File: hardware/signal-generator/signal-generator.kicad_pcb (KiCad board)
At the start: 4 copper layers, 135 parts, among them J1 AVR-ISP-6, J10 Output_Conn, J11 SD_Card_Conn, J12 TP_Conn, J13 LCD_Conn, J2 AVR_SPI, J3 PORT_G, J4 PORT_F, J5 PORT_E, J6 PORT_A, J7 PORT_C, J8 AREF, J9 Power_Supply_Rails, Q1 AP2310GN, Q2 AP2310GN, Q3 AP2310GN, Q4 AP2310GN, Q5 AP2310GN, Q6 AP2310GN, Q7 AP2310GN, Q8 AP2310GN, Q9 AP2310GN, SW1 RESET_BUTTON, U1 74HC04, U10 MCP23017-E/SO, U11 AD9764AR, U12 TS4061AICT-1.25, U13 74HC4040, U14 74HC4040, U15 MCP4651-502E/ST, U16 AZ431AN-A, U17 AD8021ARZ, U18 MCP4551-103E/MS, U19 AD8021ARZ, U2 74HC08, U20 AD8021ARZ, U21 AD8021ARZ, U3 74HC08, U4 74HC30, U5 ATmega2561-16AU, U6 ADP7142AUJZ-5.0, U7 TC1017-3.3VCTTR, U8 DS1085Z-10+, U9 CY7C1021D-10ZSXI, Y1 16MHz

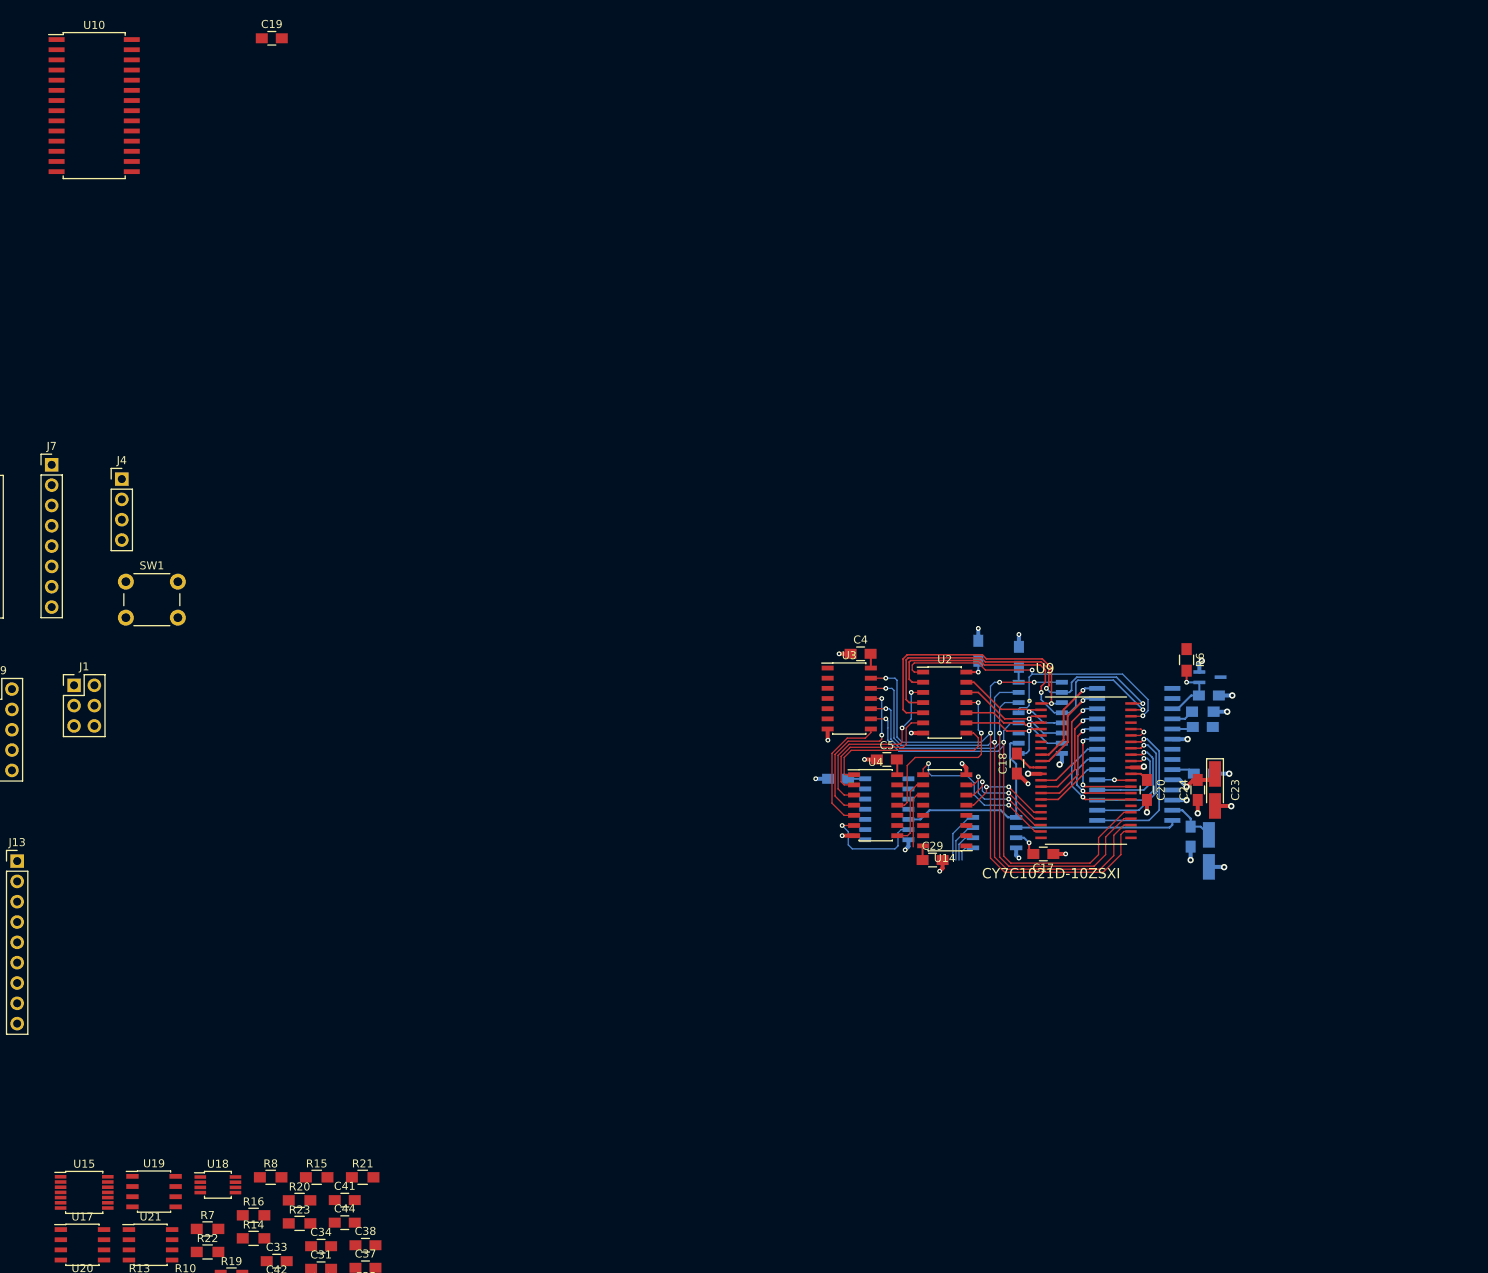
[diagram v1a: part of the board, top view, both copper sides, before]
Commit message: [Signal Generator] Rework DDS system PCB layout
The previous layout of the DDS system had its components rather
awkwardly positioned. Furthermore, it did not take into account the
distinction of the digital and analog grounds, as well as their star
ground connection.
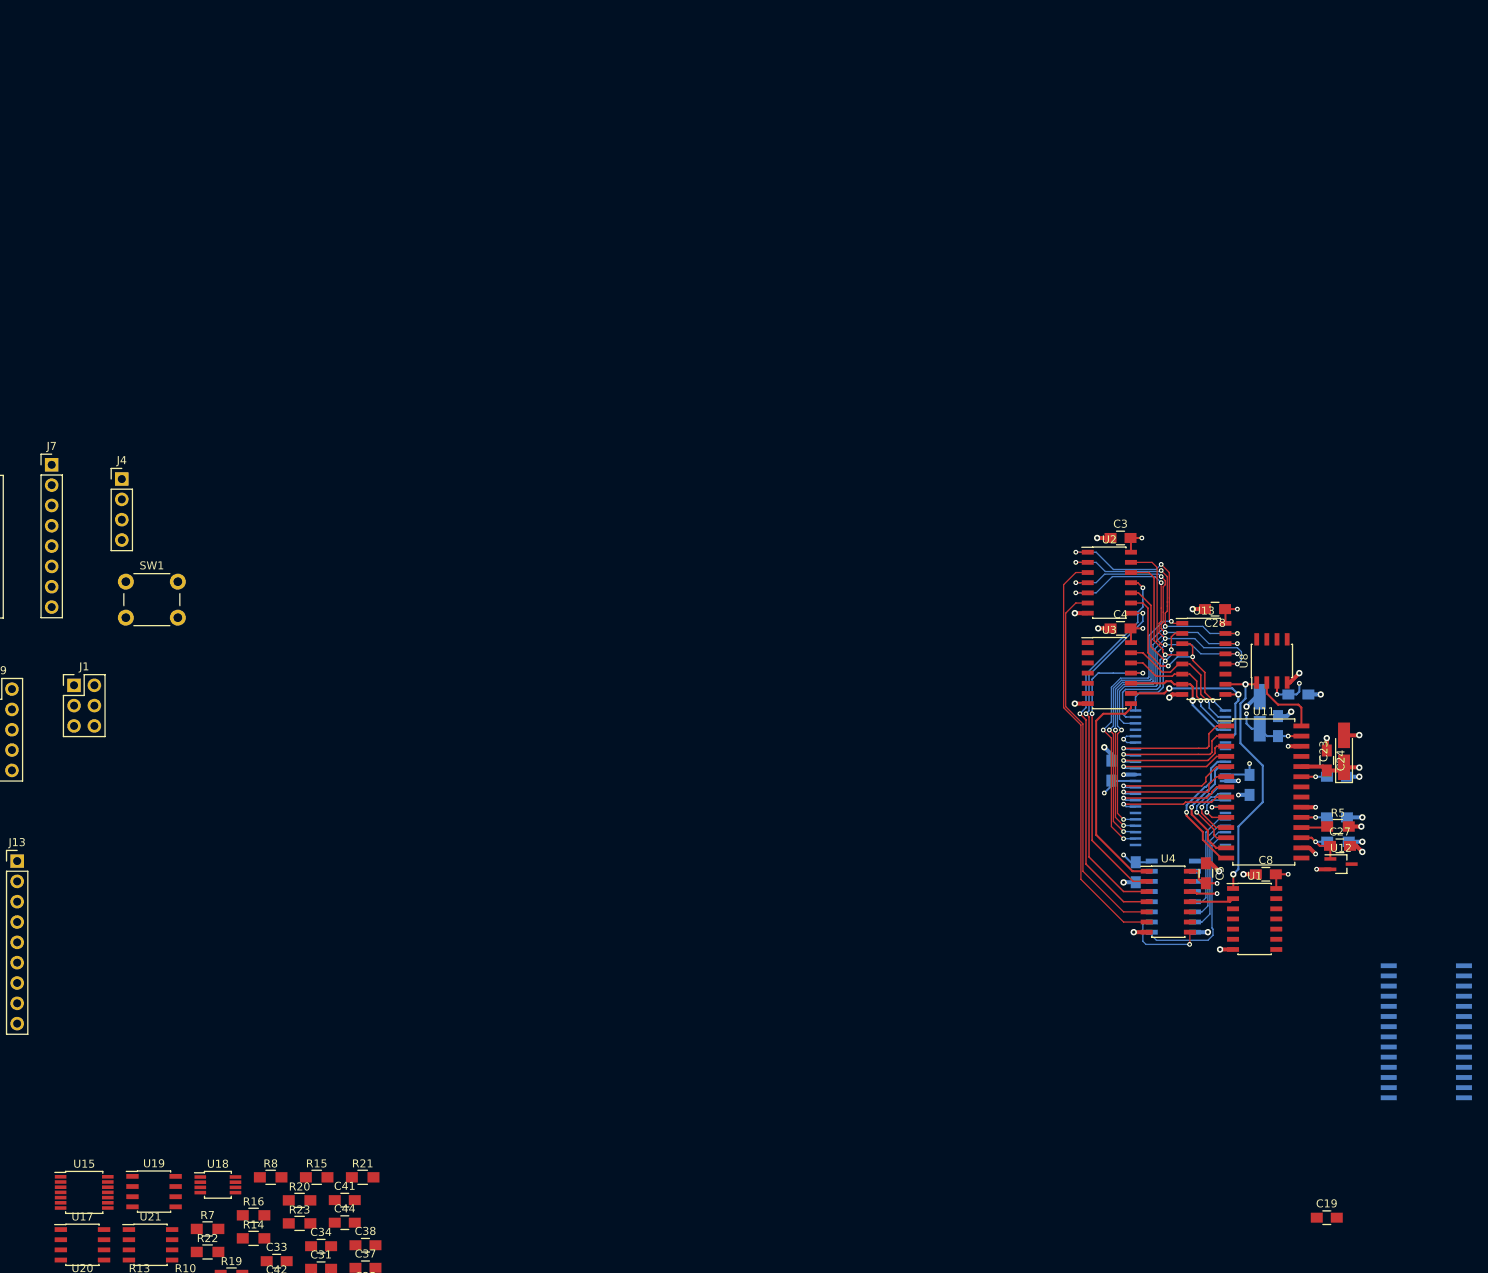
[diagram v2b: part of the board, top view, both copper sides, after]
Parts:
- C17, C18, C20, C29, R6, U10, U14, U9: moved to B.Cu
- C27, C28, C3, C8, R5, U1, U11, U12, U13, U8: moved to F.Cu
- moved U10 202.8 mm to (177.9, 102.6), turned to 180 degrees
- moved C19 197.8 mm to (165.5, 125.9)
- moved C8 54.8 mm to (157.9, 82.9)
- moved U1 48.0 mm to (156.5, 88.5), turned to 0 degrees
- moved C5 42.3 mm to (150.4, 82.8), turned to 270 degrees
- moved U8 40.8 mm to (158.6, 56.3), turned to 90 degrees
- moved U4 38.5 mm to (145.7, 86.4)
- moved C17 37.6 mm to (161.9, 60.5)
- moved U3 32.7 mm to (138.3, 57.8)
- moved C4 32.6 mm to (139.7, 52.2)
- moved U14 30.5 mm to (146.3, 85.7)
- moved R6 29.6 mm to (166.9, 78.9), turned to 180 degrees
- moved C18 29.2 mm to (155.8, 71.8)
- moved U12 28.5 mm to (167.3, 81.7)
- moved U2 25.5 mm to (138.3, 46.5)
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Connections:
- U1 pad 1: Net-(U1-Pad1) -> /~CP
- U1 pad 2: Net-(U1-Pad2) -> /DDS System/16-bit Counter/CP2I6
- U1 pad 5: /~CP -> Net-(U1-Pad5)
- U1 pad 6: /DDS System/16-bit Counter/CP2I6 -> Net-(U1-Pad6)
- U2 pad 1: /DDS System/16-bit Counter/Q7 -> /DDS System/16-bit Counter/Q11
- U2 pad 10: /DDS System/16-bit Counter/Q1 -> /DDS System/16-bit Counter/Q5
- U2 pad 11: /DDS System/16-bit Counter/CP2I0 -> /DDS System/16-bit Counter/CP2I3
- U2 pad 12: /DDS System/16-bit Counter/Q2 -> /DDS System/16-bit Counter/Q6
- U2 pad 13: /DDS System/16-bit Counter/Q3 -> /DDS System/16-bit Counter/Q7
- U2 pad 2: /DDS System/16-bit Counter/Q6 -> /DDS System/16-bit Counter/Q10
- U2 pad 3: /DDS System/16-bit Counter/CP2I3 -> /DDS System/16-bit Counter/CP2I5
- U2 pad 4: /DDS System/16-bit Counter/Q5 -> /DDS System/16-bit Counter/Q9
- U2 pad 5: /DDS System/16-bit Counter/Q4 -> /DDS System/16-bit Counter/Q8
- U2 pad 6: /DDS System/16-bit Counter/CP2I2 -> /DDS System/16-bit Counter/CP2I4
- U2 pad 8: /DDS System/16-bit Counter/CP2I1 -> /DDS System/16-bit Counter/CP2I2
- U2 pad 9: /DDS System/16-bit Counter/Q0 -> /DDS System/16-bit Counter/Q4
- U3 pad 10: /DDS System/16-bit Counter/Q9 -> /DDS System/16-bit Counter/Q1
- U3 pad 11: /DDS System/16-bit Counter/CP2I4 -> /DDS System/16-bit Counter/CP2I1
- U3 pad 12: /DDS System/16-bit Counter/Q10 -> /DDS System/16-bit Counter/Q2
- U3 pad 13: /DDS System/16-bit Counter/Q11 -> /DDS System/16-bit Counter/Q3
- U3 pad 8: /DDS System/16-bit Counter/CP2I5 -> /DDS System/16-bit Counter/CP2I0
- U3 pad 9: /DDS System/16-bit Counter/Q8 -> /DDS System/16-bit Counter/Q0
- U4 pad 1: /DDS System/16-bit Counter/CP2I1 -> /DDS System/16-bit Counter/CP2I0
- U4 pad 11: /DDS System/16-bit Counter/CP2I0 -> /DDS System/16-bit Counter/CP2I6
- U4 pad 2: /DDS System/16-bit Counter/CP2I2 -> /DDS System/16-bit Counter/CP2I1
- U4 pad 3: /DDS System/16-bit Counter/CP2I3 -> /DDS System/16-bit Counter/CP2I2
- U4 pad 4: /DDS System/16-bit Counter/CP2I4 -> /DDS System/16-bit Counter/CP2I3
- U4 pad 5: /DDS System/16-bit Counter/CP2I5 -> /DDS System/16-bit Counter/CP2I4
- U4 pad 6: /DDS System/16-bit Counter/CP2I6 -> /DDS System/16-bit Counter/CP2I5
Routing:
- net /DDS System/16-bit Counter/CP2I5: track 16.0 -> 51.8 mm
- net /DDS System/16-bit Counter/CP2I3: track 23.4 -> 49.4 mm
- net /DDS System/16-bit Counter/CP2I2: track 18.1 -> 44.1 mm, vias 0 -> 2
- net /DDS System/16-bit Counter/CP2I4: track 21.1 -> 46.5 mm, vias 2 -> 0
- net +5VD: track 28.6 -> 48.9 mm, vias 2 -> 13
- net /DDS System/16-bit Counter/Q5: track 44.8 -> 24.8 mm
- net /DDS System/16-bit Counter/Q11: track 75.5 -> 58.3 mm, vias 4 -> 5
- net /DDS System/16-bit Counter/Q6: track 45.4 -> 29.2 mm, vias 2 -> 1
- net /DDS System/16-bit Counter/CP2I1: track 23.5 -> 37.3 mm, vias 0 -> 2
- net /DDS System/DACCLK: track 20.2 -> 8.70 mm
- net Net-(U10-Pad4): track 4.25 -> 15.7 mm
- net /DDS System/16-bit Counter/Q4: track 35.6 -> 26.1 mm, vias 1 -> 3
- net Net-(U10-Pad28): track 12.6 -> 3.49 mm
- net /DDS System/16-bit Counter/CP2I6: track 13.9 -> 5.55 mm, vias 1 -> 0
- net /DDS System/16-bit Counter/Q0: track 14.2 -> 22.1 mm, vias 1 -> 2
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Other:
- net class Analog Signal: clearance 0.15 -> 0.127; trace_width 0.25 -> 0.254
- net class Analog Supply: clearance 0.15 -> 0.127; trace_width 0.5 -> 0.508
- net class Digital HS Signal: trace_width 0.2 -> 0.1905
- net class Digital Signal: trace_width 0.15 -> 0.127
- net class Digital Supply: clearance 0.15 -> 0.1127; trace_width 0.25 -> 0.254
- net class Digital UHS Signal: clearance 0.2 -> 0.1905; trace_width 0.25 -> 0.254
- rule trace_min: 0.127 -> 0.0889
- rule via_min_drill: 0.3 -> 0.2
- rule via_min_size: 0.4 -> 0.45

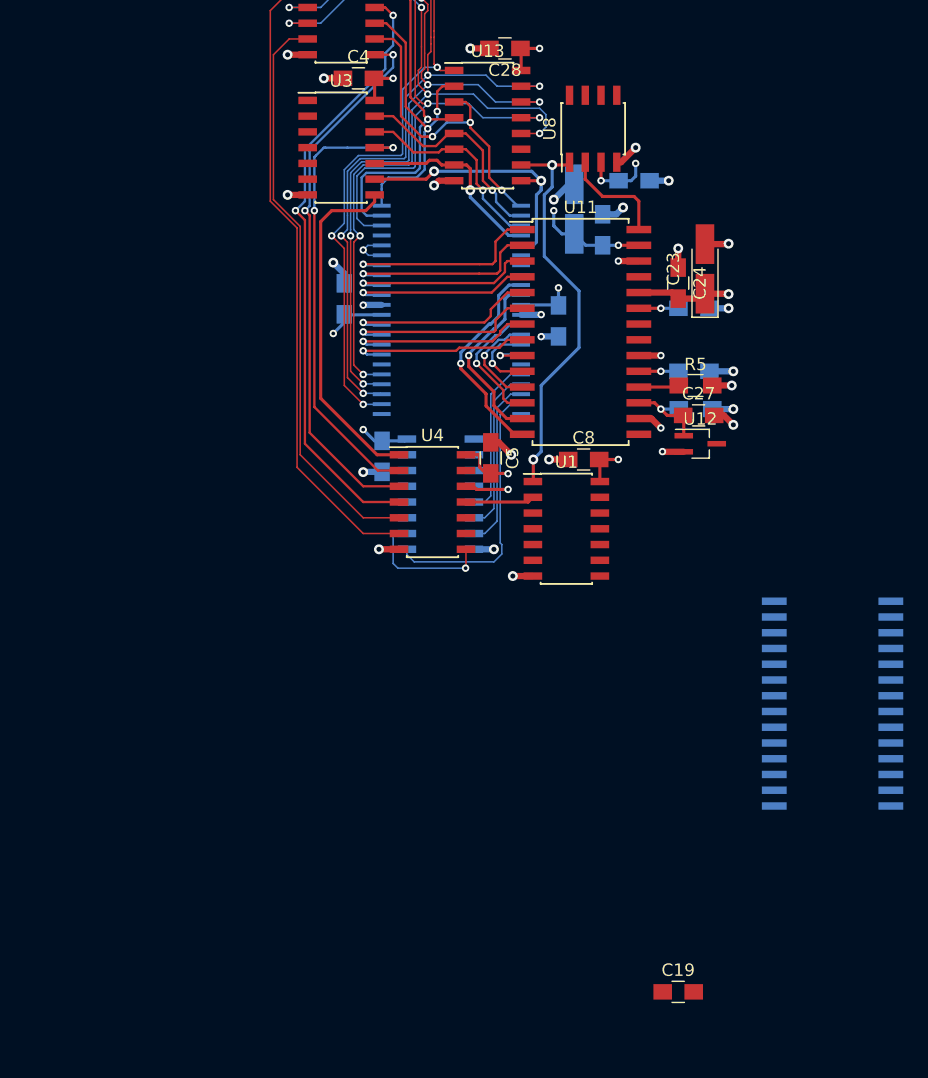
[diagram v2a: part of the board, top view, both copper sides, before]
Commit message: [Signal Generator] Complete DDS system layout
The I/O expander (MCP23017) has been added and routed.
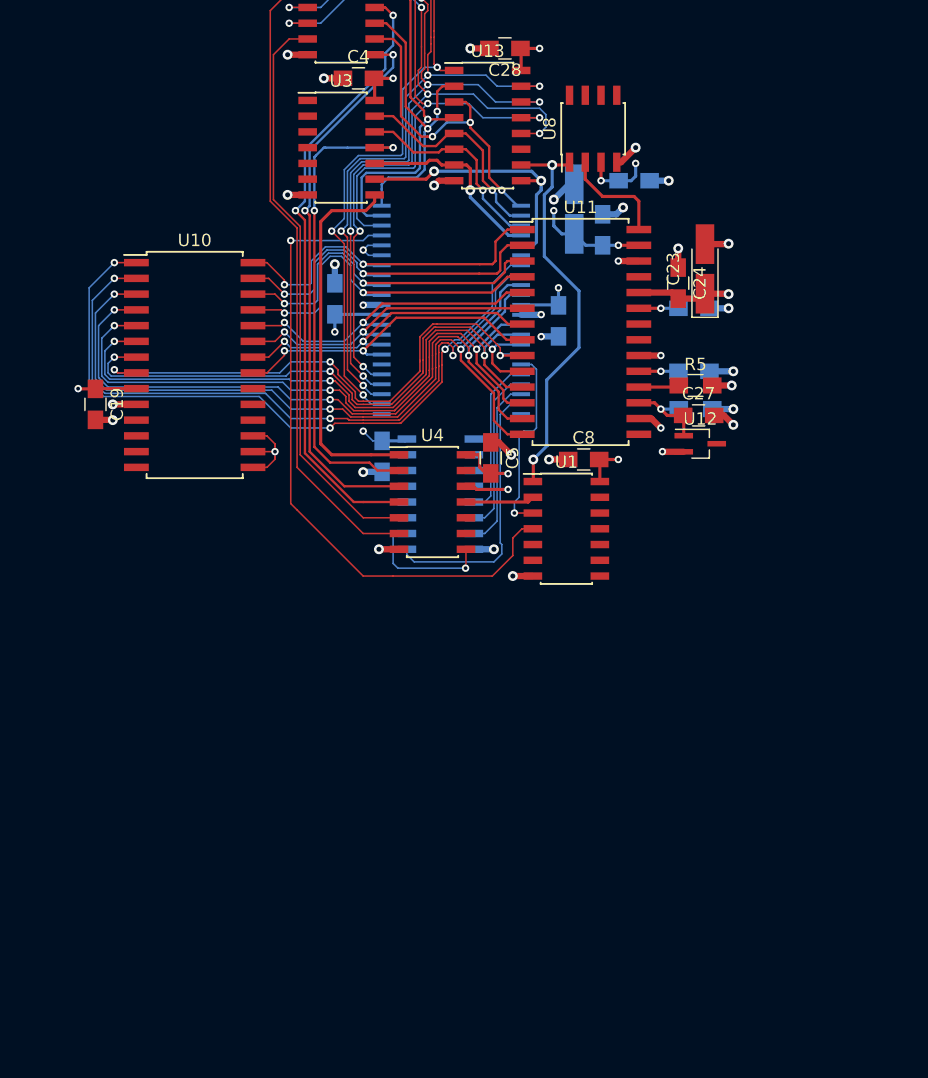
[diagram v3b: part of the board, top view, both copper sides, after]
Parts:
- U10: moved to F.Cu
- moved C19 66.7 mm to (118.5, 78.5), turned to 270 degrees
- moved U10 58.2 mm to (126.5, 75.3), turned to 0 degrees
- moved C20 0.76 mm to (137.8, 70.0)
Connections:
- U11 pad 1: Net-(U10-Pad8) -> Net-(U10-Pad28)
- U11 pad 10: Net-(U10-Pad27) -> Net-(U10-Pad7)
- U11 pad 11: Net-(U10-Pad26) -> Net-(U10-Pad6)
- U11 pad 12: Net-(U10-Pad25) -> Net-(U10-Pad5)
- U11 pad 13: Net-(U10-Pad24) -> Net-(U10-Pad4)
- U11 pad 14: Net-(U10-Pad23) -> Net-(U10-Pad3)
- U11 pad 2: Net-(U10-Pad7) -> Net-(U10-Pad27)
- U11 pad 3: Net-(U10-Pad6) -> Net-(U10-Pad26)
- U11 pad 4: Net-(U10-Pad5) -> Net-(U10-Pad25)
- U11 pad 5: Net-(U10-Pad4) -> Net-(U10-Pad24)
- U11 pad 6: Net-(U10-Pad3) -> Net-(U10-Pad23)
- U11 pad 7: Net-(U10-Pad2) -> Net-(U10-Pad22)
- U11 pad 8: Net-(U10-Pad1) -> Net-(U10-Pad21)
- U11 pad 9: Net-(U10-Pad28) -> Net-(U10-Pad8)
- U9 pad 10: Net-(U10-Pad24) -> Net-(U10-Pad4)
- U9 pad 13: Net-(U10-Pad25) -> Net-(U10-Pad5)
- U9 pad 14: Net-(U10-Pad26) -> Net-(U10-Pad6)
- U9 pad 15: Net-(U10-Pad27) -> Net-(U10-Pad7)
- U9 pad 16: Net-(U10-Pad28) -> Net-(U10-Pad8)
- U9 pad 29: Net-(U10-Pad1) -> Net-(U10-Pad21)
- U9 pad 30: Net-(U10-Pad2) -> Net-(U10-Pad22)
- U9 pad 31: Net-(U10-Pad3) -> Net-(U10-Pad23)
- U9 pad 32: Net-(U10-Pad4) -> Net-(U10-Pad24)
- U9 pad 35: Net-(U10-Pad5) -> Net-(U10-Pad25)
- U9 pad 36: Net-(U10-Pad6) -> Net-(U10-Pad26)
- U9 pad 37: Net-(U10-Pad7) -> Net-(U10-Pad27)
- U9 pad 38: Net-(U10-Pad8) -> Net-(U10-Pad28)
- U9 pad 7: Net-(U10-Pad21) -> Net-(U10-Pad1)
- U9 pad 8: Net-(U10-Pad22) -> Net-(U10-Pad2)
- U9 pad 9: Net-(U10-Pad23) -> Net-(U10-Pad3)
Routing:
- net Net-(U1-Pad4): track 0.00 -> 53.1 mm, vias 0 -> 1
- net Net-(U10-Pad3): track 15.7 -> 61.9 mm, vias 1 -> 3
- net Net-(U10-Pad4): track 15.7 -> 58.7 mm, vias 1 -> 3
- net Net-(U10-Pad1): track 14.8 -> 56.6 mm, vias 1 -> 3
- net Net-(U10-Pad2): track 15.1 -> 55.6 mm, vias 1 -> 3
- net Net-(U10-Pad5): track 14.9 -> 53.6 mm, vias 1 -> 3
- net Net-(U10-Pad6): track 15.5 -> 50.8 mm, vias 1 -> 3
- net Net-(U10-Pad7): track 16.2 -> 47.2 mm, vias 1 -> 3
- net Net-(U10-Pad8): track 16.4 -> 44.4 mm, vias 1 -> 3
- net Net-(U10-Pad21): track 0.00 -> 26.1 mm, vias 0 -> 2
- net Net-(U10-Pad28): track 3.49 -> 29.2 mm, vias 1 -> 2
- net Net-(U10-Pad22): track 0.00 -> 25.6 mm, vias 0 -> 2
- net Net-(U10-Pad27): track 6.14 -> 29.3 mm, vias 1 -> 2
- net Net-(U10-Pad26): track 8.27 -> 29.6 mm, vias 1 -> 2
- net Net-(U10-Pad25): track 10.7 -> 29.6 mm, vias 1 -> 2
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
